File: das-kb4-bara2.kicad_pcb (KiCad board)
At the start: 2 copper layers, 58 parts, among them J1 USB_A, J2 USB_A, J3 Conn_01x26_Socket, J4 USB_C_Receptacle_USB2.0, J5 Conn_ARM_JTAG_SWD_10, SW1 PWR, SW2 MUTE, SW3 PREV, SW4 PLAY_PAUSE, SW5 NEXT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

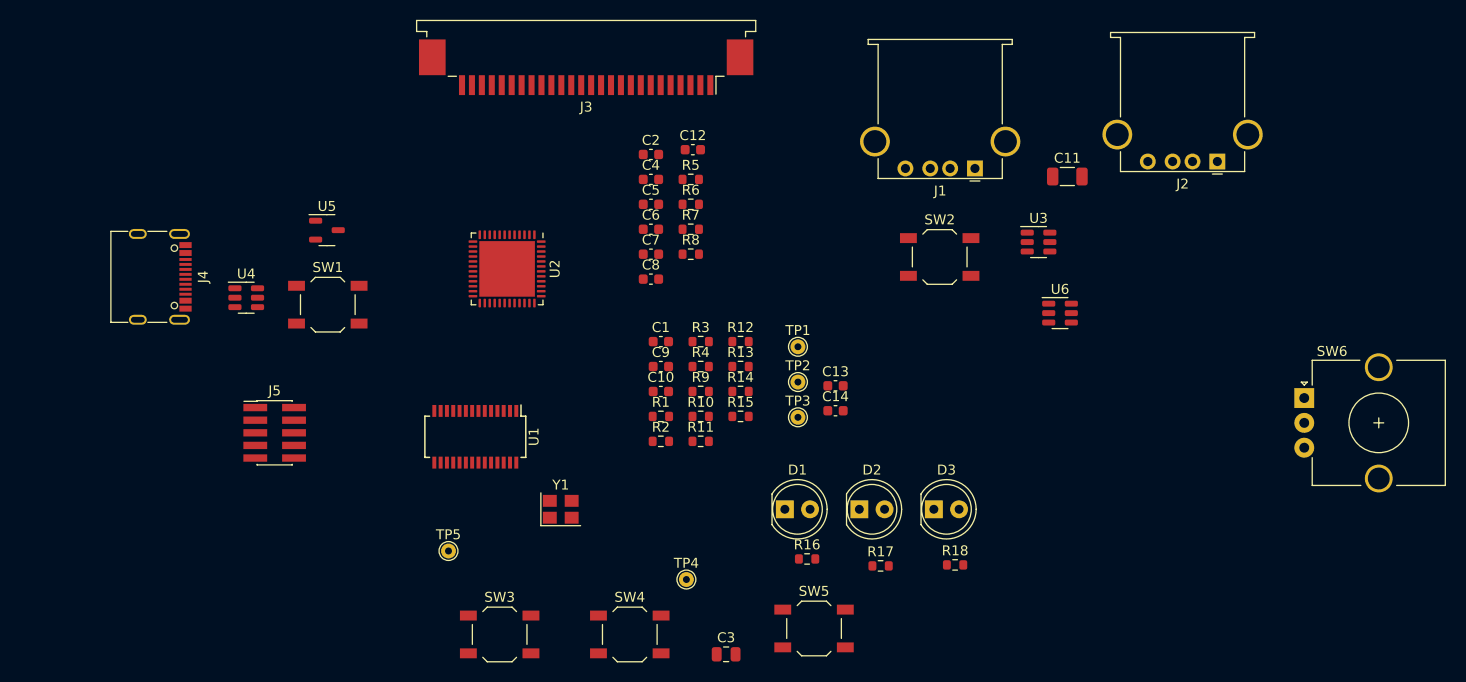
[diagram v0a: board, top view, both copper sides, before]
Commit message: import board outline and lock fixed items
No routing, just rough placement of all the fixed items.
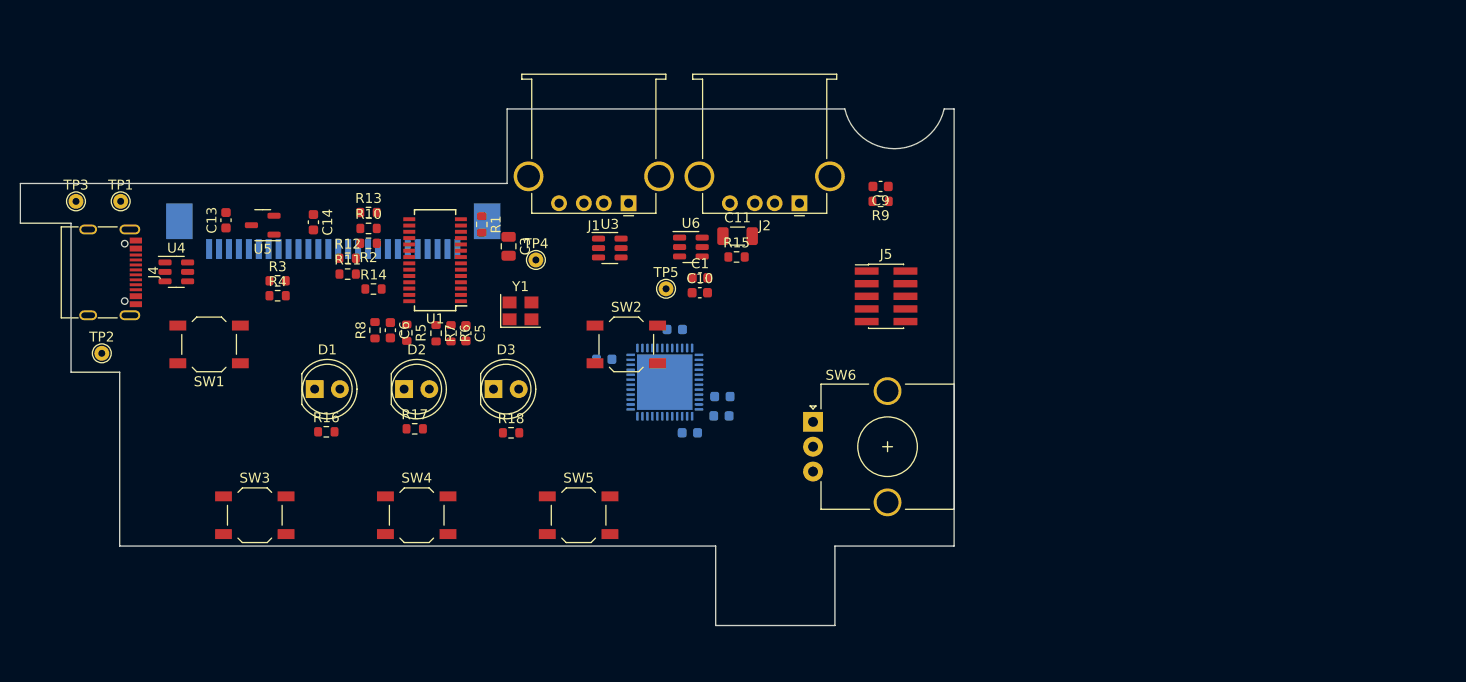
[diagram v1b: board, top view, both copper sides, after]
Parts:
- C12, C2, C4, C7, C8, J3, U2: moved to B.Cu
- moved TP3 75.9 mm to (99.0, 90.6)
- moved TP2 70.1 mm to (101.6, 105.9)
- moved TP1 69.7 mm to (103.5, 90.6)
- moved C13 63.6 mm to (114.1, 92.5), turned to 90 degrees
- moved J5 63.1 mm to (180.6, 100.2)
- moved C14 55.9 mm to (122.9, 92.7), turned to -90 degrees
- moved R16 50.1 mm to (124.2, 113.8)
- moved SW6 49.5 mm to (173.2, 112.8)
- moved R17 48.9 mm to (133.1, 113.5)
- moved D1 48.9 mm to (123.0, 109.5)
- moved D2 47.4 mm to (132.0, 109.5)
- moved R18 46.6 mm to (142.8, 113.9)
- moved C3 46.5 mm to (142.6, 95.1), turned to -90 degrees
- moved D3 46.0 mm to (141.0, 109.5)
- moved R4 43.2 mm to (119.3, 100.1)
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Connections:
- net Net-(U1-BUSJ) renamed /usb/BUSJ
- net Net-(U1-VD33) renamed /usb/VD33
- net Net-(U6-ILIM) renamed /usb/ILIM
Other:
- board outline added: 94 x 52 mm
- copper layers 2 -> 4

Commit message: add "bonus" can transceiver ;)
this is so we can use the round 1 protos for another project...

also: replace srv05 with an alternate, also jlc preferred, but cheaper
part.  Update power budgets.

We've done some initial work with the pcb, but we're running into weird
kicad wx bugs, so we're going to save it all here, and commit, and
perhaps continue with 7.99.....
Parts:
- added D4: NUP2105L, Package_TO_SOT_SMD:SOT-23, F.Cu at (208.2, 91.0)
- added J6: Conn_02x03_Odd_Even, Connector_PinHeader_2.54mm:PinHeader_2x03_P2.54mm_Vertical, F.Cu at (200.9, 84.7)
- added R19: 10k, Resistor_SMD:R_0603_1608Metric, F.Cu at (200.6, 93.3)
- added U7: SN65HVD230, Package_SO:SOIC-8_3.9x4.9mm_P1.27mm, B.Cu at (171.8, 100.9)
- moved TP5 16.1 mm to (174.1, 95.7)
- moved U6 1.40 mm to (159.5, 95.2), turned to 90 degrees
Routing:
- net GNDPWR: track 0.00 -> 36.6 mm
- net GND: track 0.00 -> 4.31 mm, vias 0 -> 1
- added copper zone on In1.Cu, net GND

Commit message: routing progress
Just nice to make some save points every now and again.
USB seems... ok?  Still need to check 3v3 or 5v on the power pullups,
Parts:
- added C15: 100nF, Capacitor_SMD:C_0603_1608Metric, B.Cu at (167.0, 101.1)
- D4, R19: moved to B.Cu
- moved R8 43.3 mm to (170.0, 117.8), turned to 180 degrees
- moved C6 41.4 mm to (170.0, 116.3), turned to 0 degrees
- moved R5 40.8 mm to (170.0, 119.3), turned to 0 degrees
- moved R7 35.3 mm to (170.0, 110.2), turned to 0 degrees
- moved R6 34.2 mm to (170.0, 111.7), turned to 0 degrees
- moved C5 33.1 mm to (170.0, 113.2), turned to 0 degrees
- moved J5 30.3 mm to (170.0, 128.6), turned to 90 degrees
- moved R19 29.0 mm to (174.0, 105.0)
- moved TP4 28.1 mm to (158.5, 121.3)
- moved D4 26.5 mm to (184.9, 103.5)
- moved J6 18.3 mm to (185.8, 95.0), turned to 180 degrees
- moved R3 17.5 mm to (103.2, 105.5), turned to -90 degrees
- moved R4 15.5 mm to (104.8, 105.5), turned to -90 degrees
- moved C3 14.7 mm to (128.2, 98.4), turned to 180 degrees
- moved C10 13.2 mm to (148.7, 98.3), turned to -90 degrees
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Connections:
- D4 pad 1: Net-(J6-Pin_1) -> /keys_mcu/CANH
- J6 pad 1: Net-(J6-Pin_1) -> /keys_mcu/CANH
- U1 pad 10: UMCU_N -> /usb/UDS1N
- U1 pad 11: UMCU_P -> /usb/UDS1P
- U1 pad 6: /usb/UDS2N -> UMCU_N
- U1 pad 7: /usb/UDS2P -> UMCU_P
- U1 pad 8: /usb/UDS1N -> /usb/UDS2N
- U1 pad 9: /usb/UDS1P -> /usb/UDS2P
- U3 pad 3: /usb/UDS1N -> /usb/UDS2P
- U3 pad 4: /usb/UDS2P -> /usb/UDS2N
- U3 pad 6: /usb/UDS2N -> /usb/UDS1N
- U4 pad 1: /usb/UUPN -> unconnected-(U4-IO1-Pad1)
- U4 pad 3: /usb/UUPP -> /usb/UUPN
- U4 pad 4: unconnected-(U4-IO3-Pad4) -> /usb/UUPP
- U7 pad 7: Net-(J6-Pin_1) -> /keys_mcu/CANH
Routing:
- net +3V3: track 0.00 -> 45.2 mm, vias 0 -> 8
- net /keys_mcu/SW3: track 0.00 -> 37.1 mm
- net /usb/UUPP: track 0.00 -> 34.7 mm
- net /usb/UUPN: track 0.00 -> 34.7 mm
- net /usb/UDS2N: track 0.00 -> 34.3 mm
- net /usb/UDS2P: track 0.00 -> 33.6 mm
- net /usb/PWR_OC: track 0.00 -> 33.4 mm
- net UMCU_P: track 0.00 -> 26.6 mm, vias 0 -> 1
- net UMCU_N: track 0.00 -> 26.1 mm, vias 0 -> 1
- net /usb/PWR_EN: track 0.00 -> 25.9 mm
- net /keys_mcu/SW4: track 0.00 -> 21.2 mm
- net GND: track 4.31 -> 23.1 mm, vias 1 -> 4
- net /keys_mcu/ENC_A: track 0.00 -> 17.5 mm, vias 0 -> 1
- net /keys_mcu/ENC_B: track 0.00 -> 17.3 mm, vias 0 -> 1
- net /usb/UDS1N: track 0.00 -> 16.5 mm
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- added copper zone on In2.Cu, net +3V3
- added copper zone on F.Cu, net +5V
- added copper zone on In2.Cu, net +5V
- added copper zone on In2.Cu, net VBUS

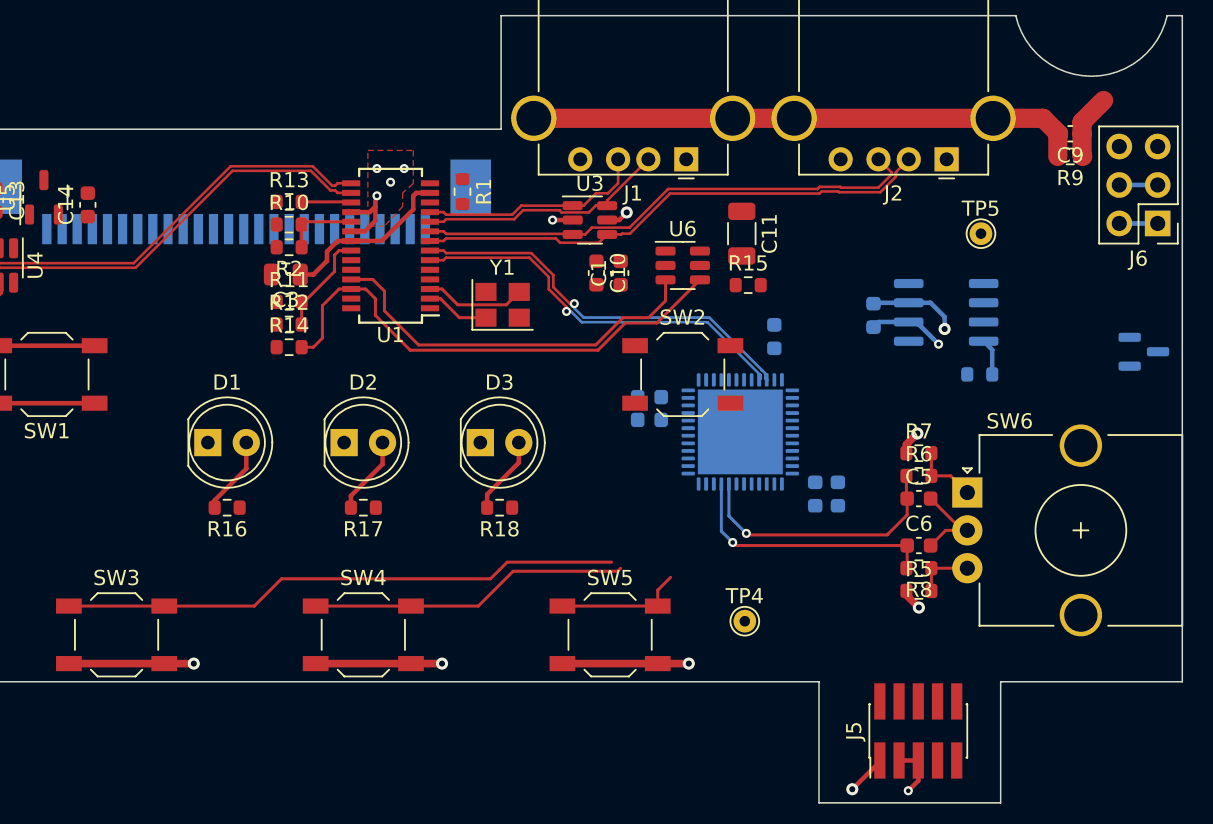
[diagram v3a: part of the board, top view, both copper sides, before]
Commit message: cleanup schematic, break out most of it
Broke it all out to the right places, now I can go and shuffle all the
labels to make it line up.  Thankfully we can just "freely" route the
keybaord matrix pins!
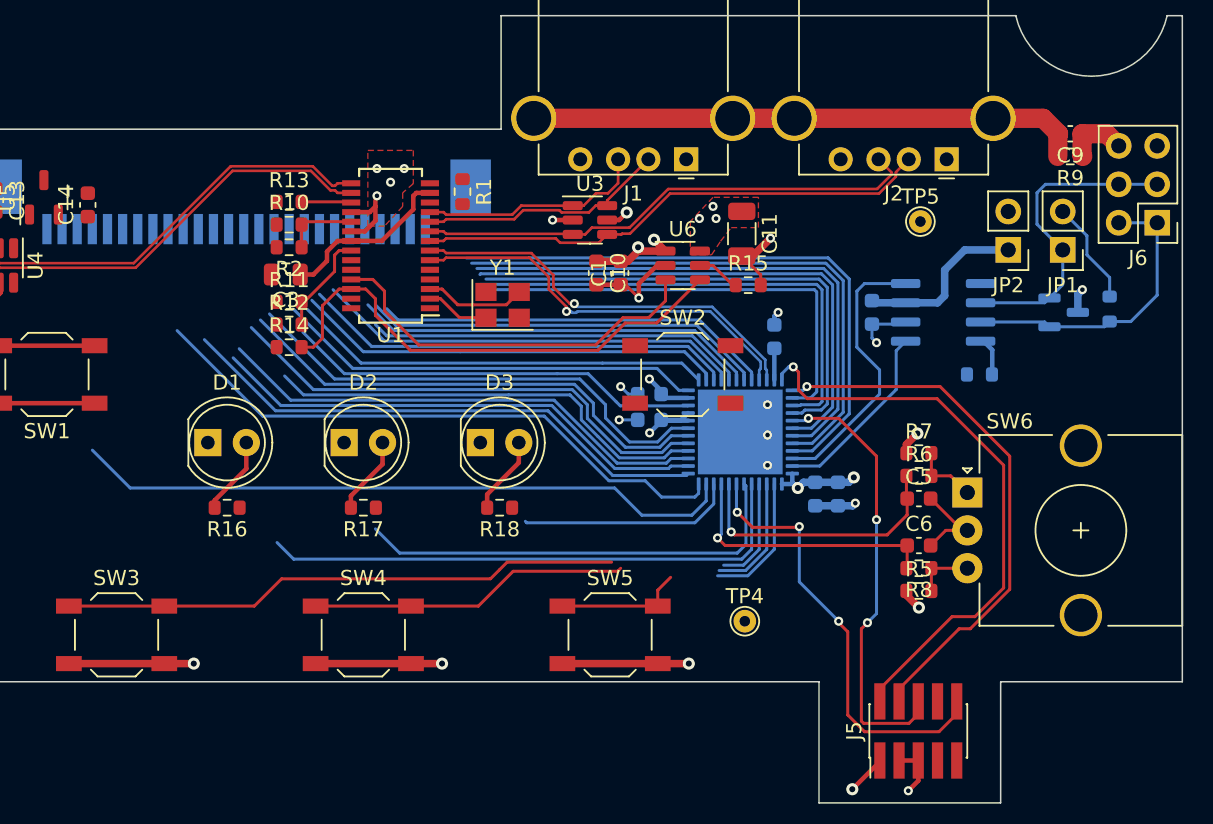
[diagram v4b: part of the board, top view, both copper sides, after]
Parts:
- added JP1: Jumper_2_Open, Connector_PinHeader_2.54mm:PinHeader_1x02_P2.54mm_Vertical, F.Cu at (179.5, 96.8)
- added JP2: Jumper_2_Open, Connector_PinHeader_2.54mm:PinHeader_1x02_P2.54mm_Vertical, F.Cu at (175.9, 96.8)
- added R20: 120, Resistor_SMD:R_0603_1608Metric, B.Cu at (182.6, 100.7)
- moved D4 5.90 mm to (179.6, 100.9)
- moved TP5 4.08 mm to (170.1, 94.9)
- moved C15 0.22 mm to (166.9, 100.9)
- moved U7 0.20 mm to (171.6, 100.9)
- moved C7 0.20 mm to (152.2, 106.3)
- moved J6 0.06 mm to (185.7, 95.0)
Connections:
- net /keys_mcu/Any_thing renamed /can/CAN_SHUTDOWN
- net /keys_mcu/CANH renamed /can/CANH
- net /keys_mcu/CANL renamed /can/CANL
- C15 pad 2: +3V3 -> /can/Local3v3
- U2 pad 10: /keys_mcu/CM17 -> /keys_mcu/SCROLL_LOCK
- U2 pad 11: /keys_mcu/CM18 -> /keys_mcu/SW1
- U2 pad 16: /keys_mcu/SW2 -> /keys_mcu/CM26
- U2 pad 2: /keys_mcu/SW3 -> /keys_mcu/SW5
- U2 pad 29: /keys_mcu/CAPS_LOCK -> /keys_mcu/CM10
- U2 pad 38: /keys_mcu/CM26 -> /keys_mcu/CM18
- U2 pad 39: /keys_mcu/SCROLL_LOCK -> /keys_mcu/CM17
- U2 pad 4: /keys_mcu/SW5 -> /keys_mcu/SW3
- U2 pad 46: /keys_mcu/SW1 -> /keys_mcu/SW2
- U2 pad 47: /keys_mcu/CM10 -> /keys_mcu/CM9
- U2 pad 6: /keys_mcu/CM9 -> /keys_mcu/CAPS_LOCK
- U4 pad 3: /usb/UUPN -> /usb/UUPP
- U4 pad 4: /usb/UUPP -> /usb/UUPN
- U7 pad 1: /keys_mcu/CM11 -> /keys_mcu/CM9
- U7 pad 3: +3V3 -> /can/Local3v3
- U7 pad 4: /keys_mcu/CM10 -> /keys_mcu/SW2
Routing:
- net /keys_mcu/SW1: track 6.30 -> 50.1 mm
- net /keys_mcu/CM19: track 0.00 -> 39.7 mm
- net /keys_mcu/CM8: track 0.00 -> 39.6 mm
- net /keys_mcu/SWD_IO: track 0.00 -> 38.5 mm, vias 0 -> 1
- net /keys_mcu/CM7: track 0.00 -> 37.9 mm
- net /keys_mcu/NUM_LOCK: track 0.00 -> 36.4 mm
- net /keys_mcu/CM6: track 0.00 -> 36.3 mm
- net /keys_mcu/SWD_CLK: track 0.00 -> 36.0 mm, vias 0 -> 1
- net /keys_mcu/CM20: track 0.00 -> 35.7 mm
- net /keys_mcu/CM5: track 0.00 -> 34.9 mm
- net /keys_mcu/CM21: track 0.00 -> 33.2 mm
- net /keys_mcu/CM2: track 0.00 -> 33.1 mm
- net /keys_mcu/CM1: track 0.00 -> 33.0 mm
- net /keys_mcu/CM22: track 0.00 -> 32.9 mm
- net /keys_mcu/CM3: track 0.00 -> 32.5 mm
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- added copper zone on F.Cu, net VBUS

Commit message: unrouted: 0
Juggled all the key matrix IOs and reviewed "all" outstanding TODOs

left: add another cap for downstream Vbus.  it's free, and can only
help.

left: lots of silk?
left: place as much free io to pads as can be easily done, for
test/board reuse.
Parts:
- removed J6: Conn_02x03_Odd_Even, Connector_PinHeader_2.54mm:PinHeader_2x03_P2.54mm_Vertical
- removed TP5: TestPoint, TestPoint:TestPoint_THTPad_D1.5mm_Drill0.7mm
- added J7: Conn_02x04_Odd_Even, Connector_PinHeader_2.54mm:PinHeader_2x04_P2.54mm_Vertical, F.Cu at (185.7, 95.0)
- C13, C14, R16, R17, R18, U5: moved to B.Cu
- moved TP4 36.5 mm to (139.5, 90.1)
- moved C13 11.2 mm to (117.0, 101.4)
- moved C14 8.18 mm to (112.0, 101.4)
- moved U5 7.84 mm to (114.5, 100.8)
- moved R1 0.58 mm to (140.1, 92.4), turned to 0 degrees
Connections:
- J3 pad 1: /keys_mcu/CM1 -> /keys_mcu/CM19
- J3 pad 10: /keys_mcu/CM10 -> /keys_mcu/CM12
- J3 pad 11: /keys_mcu/CM11 -> /keys_mcu/CM13
- J3 pad 12: /keys_mcu/CM12 -> /keys_mcu/CM14
- J3 pad 13: /keys_mcu/CM13 -> /keys_mcu/CM15
- J3 pad 14: /keys_mcu/CM14 -> /keys_mcu/CM16
- J3 pad 15: /keys_mcu/CM15 -> /keys_mcu/CM10
- J3 pad 16: /keys_mcu/CM16 -> /keys_mcu/CM23
- J3 pad 17: /keys_mcu/CM17 -> /keys_mcu/CM24
- J3 pad 18: /keys_mcu/CM18 -> /keys_mcu/CM25
- J3 pad 19: /keys_mcu/CM19 -> /keys_mcu/CM18
- J3 pad 2: /keys_mcu/CM2 -> /keys_mcu/CM20
- J3 pad 20: /keys_mcu/CM20 -> /keys_mcu/CM17
- J3 pad 21: /keys_mcu/CM21 -> /keys_mcu/CM1
- J3 pad 22: /keys_mcu/CM22 -> /keys_mcu/CM5
- J3 pad 23: /keys_mcu/CM23 -> /keys_mcu/CM6
- J3 pad 24: /keys_mcu/CM24 -> /keys_mcu/CM7
- J3 pad 25: /keys_mcu/CM25 -> /keys_mcu/CM8
- J3 pad 26: /keys_mcu/CM26 -> /keys_mcu/CM9
- J3 pad 3: /keys_mcu/CM3 -> /keys_mcu/CM21
- J3 pad 4: /keys_mcu/CM4 -> /keys_mcu/CM22
- J3 pad 5: /keys_mcu/CM5 -> /keys_mcu/CM26
- J3 pad 6: /keys_mcu/CM6 -> /keys_mcu/CM2
- J3 pad 7: /keys_mcu/CM7 -> /keys_mcu/CM3
- J3 pad 8: /keys_mcu/CM8 -> /keys_mcu/CM4
- J3 pad 9: /keys_mcu/CM9 -> /keys_mcu/CM11
- R13 pad 1: +3V3 -> +5V
- R14 pad 1: +3V3 -> +5V
- R19 pad 1: /can/CAN_SHUTDOWN -> /keys_mcu/CM8
- U4 pad 3: /usb/UUPP -> /usb/UUPN
- U4 pad 4: /usb/UUPN -> /usb/UUPP
- Y1 pad 2: unconnected-(Y1-Pad2) -> GND
- Y1 pad 4: unconnected-(Y1-Pad4) -> GND
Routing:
- net /keys_mcu/CM9: track 12.4 -> 53.8 mm
- net GND: track 40.6 -> 68.6 mm, vias 14 -> 28
- net /keys_mcu/SW2: track 18.4 -> 38.0 mm, vias 0 -> 1
- net +3V3: track 65.9 -> 83.7 mm, vias 11 -> 15
- net +5V: track 21.2 -> 37.6 mm, vias 10 -> 12
- net /keys_mcu/CM26: track 29.6 -> 45.2 mm
- net /keys_mcu/CM21: track 33.2 -> 47.4 mm
- net /keys_mcu/CM22: track 32.9 -> 46.4 mm
- net /keys_mcu/CM8: track 39.6 -> 52.4 mm, vias 0 -> 2
- net /keys_mcu/CM20: track 35.7 -> 48.6 mm
- net /keys_mcu/CM18: track 30.5 -> 43.0 mm
- net /keys_mcu/CM17: track 32.2 -> 44.5 mm
- net /keys_mcu/CM11: track 27.5 -> 39.6 mm
- net /keys_mcu/CM19: track 39.7 -> 51.5 mm
- net /keys_mcu/CM2: track 33.1 -> 44.1 mm
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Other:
- board text added: "Put more headers here"

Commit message: shuffled, added bonus, silked up...
Nearly there..?
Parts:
- added C16: 100uF, Capacitor_SMD:C_1206_3216Metric, F.Cu at (160.7, 95.7)
- added J6: Conn_01x06_Socket, Connector_PinHeader_2.54mm:PinHeader_1x06_P2.54mm_Vertical, F.Cu at (105.7, 110.5)
- added R21: 10k, Resistor_SMD:R_0603_1608Metric, F.Cu at (158.7, 100.6)
- R9: value 330 -> 220
- TP1: value TestPoint -> 5V
- TP2: value TestPoint -> 3v3
- TP3: value TestPoint -> GND
- TP4: value TestPoint -> VD33
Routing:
- net /keys_mcu/CM25: track 34.4 -> 78.9 mm, vias 0 -> 1
- net /keys_mcu/CM24: track 34.9 -> 77.5 mm, vias 0 -> 1
- net /keys_mcu/CM23: track 35.4 -> 73.9 mm, vias 0 -> 1
- net /keys_mcu/CM16: track 36.4 -> 73.7 mm, vias 0 -> 1
- net /keys_mcu/CM15: track 37.2 -> 73.2 mm, vias 0 -> 1
- net /keys_mcu/CM14: track 37.6 -> 70.2 mm, vias 0 -> 1
- net +3V3: track 83.7 -> 73.7 mm
- net GND: track 68.6 -> 73.3 mm, vias 28 -> 29
- net +5V: track 37.6 -> 36.6 mm, vias 12 -> 13
- net VBUS: vias 4 -> 6
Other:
- board text added: "120R Term"
- board text added: "5V GND CanH CanL"
- board text added: "B13 (spi2_sck) B14 (spi2-miso) B15 (spi2-mosi) A8 (i2c2-sda) A9 (i2c2-scl / U1-tx) A10 (U1-rx)"
- board text added: "Enable Can 3v3"
- board text added: "JP1 120R termination JP2 Enable CAN"
- board text added: "github.com/karlp/das-kb4-bara2 Rev: r2023-12"
- board text removed: "Put more headers here"

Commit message: fix some erc/drc
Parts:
- moved TP4 1.50 mm to (138.0, 90.0)
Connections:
- J5 pad 9: unconnected-(J5-GNDDetect-Pad9) -> GND
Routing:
- net GND: track 73.3 -> 74.6 mm, vias 29 -> 30
- net /usb/VD33: track 17.4 -> 18.5 mm
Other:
- board text removed: "JP1 120R termination JP2 Enable CAN"
